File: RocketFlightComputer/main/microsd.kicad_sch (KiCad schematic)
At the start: 1 part

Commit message: Well I added a bunch of sensors, some connectors for battery, pyro channels mosfets, etc
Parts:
- J?: value Micro_SD_Card_Det1 -> Micro_SD_Card
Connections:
- net VDD renamed +3.3V
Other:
- note added: "Max current: 150 mA"
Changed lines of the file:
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@@
   (paper "User" 135.001 119.99)
   (no_connect (at 82.55 34.925))
+  (text "Max current: 150 mA" (at 89.535 74.295 0)
+    (effects (font (size 1.778 1.5113)) (justify left bottom))
+  )
   (hierarchical_label "SD_B0_03" (shape input) (at 82.55 40.005 0) (fields_autoplaced)
     (effects (font (size 1.27 1.27)) (justify left))
@@
   )
   (hierarchical_label "SD_B0_02" (shape input) (at 82.55 42.545 0) (fields_autoplaced)
-    (effects (font (size 1.27 1.27)) (justify left))
-  )
-  (hierarchical_label "VDD" (shape input) (at 82.55 50.165 0) (fields_autoplaced)
     (effects (font (size 1.27 1.27)) (justify left))
   )
@@
     )
   )
+  (symbol (lib_id "power:+3.3V") (at 82.55 50.165 270) (unit 1)
+    (in_bom yes) (on_board yes) (dnp no)
+    (property "Reference" "#PWR059" (at 78.74 50.165 0)
+      (effects (font (size 1.27 1.27)) hide)
+    )
+    (property "Value" "+3.3V" (at 85.725 50.165 90)
+      (effects (font (size 1.27 1.27)) (justify left))
+    )
+    (property "Footprint" "" (at 82.55 50.165 0)
+      (effects (font (size 1.27 1.27)) hide)
+    )
+    (property "Datasheet" "" (at 82.55 50.165 0)
+      (effects (font (size 1.27 1.27)) hide)
+    )
+    (pin "1")
+    (instances
+      (project "main"
+        (path "/27195d1d-92b2-40df-ada5-3b20841577e7"
+          (reference "#PWR059") (unit 1)
+        )
+        (path "/27195d1d-92b2-40df-ada5-3b20841577e7/690c10de-e6bf-48ef-8c3e-99868f905c19"
+          (reference "#PWR0127") (unit 1)
+        )
+      )
+    )
+  )
   (symbol (lib_id "power:GNDREF") (at 82.55 45.085 90) (mirror x) (unit 1)
     (in_bom yes) (on_board yes) (dnp no) (fields_autoplaced)
@@
       (effects (font (size 1.27 1.27)))
     )
-    (property "Value" "Micro_SD_Card_Det1" (at 59.055 29.21 0)
+    (property "Value" "Micro_SD_Card" (at 59.055 29.21 0)
       (effects (font (size 1.27 1.27)))
     )

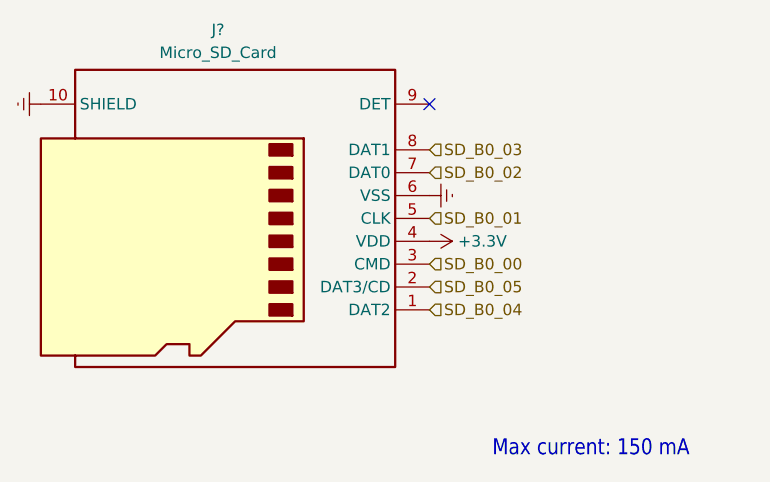
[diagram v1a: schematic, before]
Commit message: Addition of telemetry is pcb schematic
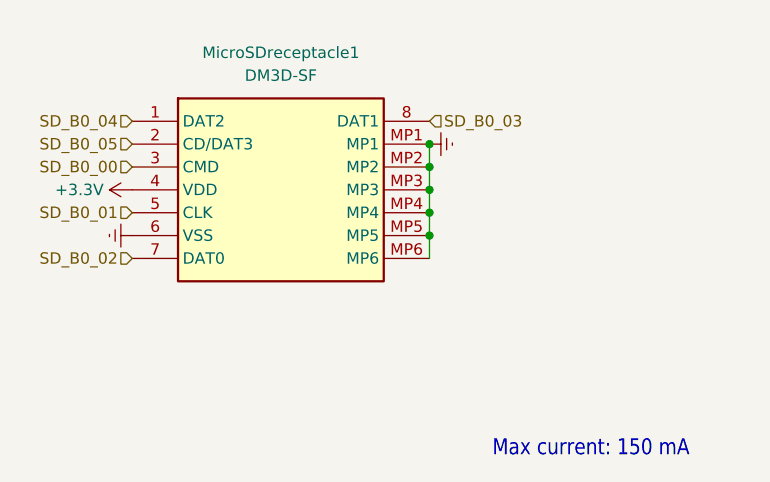
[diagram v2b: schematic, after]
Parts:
- removed J?: Micro_SD_Card, symbol Connector:Micro_SD_Card_Det1
- added MicroSDreceptacle1: DM3D-SF, DM3DSF, symbol DM3D-SF:DM3D-SF
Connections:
- net +3.3V: now also MicroSDreceptacle1.4 (VDD)
- net GNDREF: now also MicroSDreceptacle1.6 (VSS), MicroSDreceptacle1.MP1, MicroSDreceptacle1.MP2, MicroSDreceptacle1.MP3, MicroSDreceptacle1.MP4, MicroSDreceptacle1.MP5, MicroSDreceptacle1.MP6
- net SD_B0_00: now also MicroSDreceptacle1.3 (CMD)
- net SD_B0_01: now also MicroSDreceptacle1.5 (CLK)
- net SD_B0_02: now also MicroSDreceptacle1.7 (DAT0)
- net SD_B0_03: now also MicroSDreceptacle1.8 (DAT1)
- net SD_B0_04: now also MicroSDreceptacle1.1 (DAT2)
- net SD_B0_05: now also MicroSDreceptacle1.2 (CD/DAT3)
- no-connect marks 1 -> 0

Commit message: The design is getting more mature, still did not choose if doing 4 layers or 2 layers pcb, will try to add 5v for a on board camera and trace routes for reserved pins in case of usage on another vehicle
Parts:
- MicroSDreceptacle1: footprint DM3DSF -> DM3DSF:DM3DSF
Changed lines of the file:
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@@
 			)
 		)
-		(property "Footprint" "DM3DSF"
+		(property "Footprint" "DM3DSF:DM3DSF"
 			(at 78.74 131.75 0)
 			(effects

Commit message: Layout of PCB mostly done
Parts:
- DM3D-SF1: renamed from MicroSDreceptacle1; value DM3D-SF -> MicroSD
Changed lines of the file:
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@@
 		(dnp no)
 		(fields_autoplaced yes)
-		(property "Reference" "MicroSDreceptacle1"
+		(property "Reference" "DM3D-SF1"
 			(at 66.04 29.21 0)
 			(effects
@@
 					(size 1.27 1.27)
 				)
+				(hide yes)
 			)
 		)
-		(property "Value" "DM3D-SF"
+		(property "Value" "MicroSD"
 			(at 66.04 31.75 0)
 			(effects
@@
 			(project ""
 				(path "/27195d1d-92b2-40df-ada5-3b20841577e7/690c10de-e6bf-48ef-8c3e-99868f905c19"
-					(reference "MicroSDreceptacle1")
+					(reference "DM3D-SF1")
 					(unit 1)
 				)

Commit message: Addition of all components in BOM, metal mounting plates, need to check psram if its ok for signals to pass under, all components need a double check
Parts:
- DM3D-SF1: LCSC (none) -> C719027
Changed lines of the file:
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@@
 		(on_board yes)
 		(dnp no)
-		(property "Reference" "#PWR0104"
+		(property "Reference" "#PWR0109"
 			(at 53.34 44.45 0)
 			(effects
@@
 			(project "main"
 				(path "/27195d1d-92b2-40df-ada5-3b20841577e7/690c10de-e6bf-48ef-8c3e-99868f905c19"
-					(reference "#PWR0104")
+					(reference "#PWR0109")
 					(unit 1)
 				)
@@
 		(dnp no)
 		(fields_autoplaced yes)
-		(property "Reference" "#PWR0105"
+		(property "Reference" "#PWR0110"
 			(at 43.18 49.53 0)
 			(effects
@@
 			(project "main"
 				(path "/27195d1d-92b2-40df-ada5-3b20841577e7/690c10de-e6bf-48ef-8c3e-99868f905c19"
-					(reference "#PWR0105")
+					(reference "#PWR0110")
 					(unit 1)
 				)
@@
 			)
 		)
+		(property "LCSC" "C719027 "
+			(at 49.53 36.83 0)
+			(effects
+				(font
+					(size 1.27 1.27)
+				)
+				(hide yes)
+			)
+		)
 		(pin "MP1"
 		)
@@
 		(dnp no)
 		(fields_autoplaced yes)
-		(property "Reference" "#PWR0106"
+		(property "Reference" "#PWR0111"
 			(at 88.9 39.37 0)
 			(effects
@@
 			(project "main"
 				(path "/27195d1d-92b2-40df-ada5-3b20841577e7/690c10de-e6bf-48ef-8c3e-99868f905c19"
-					(reference "#PWR0106")
+					(reference "#PWR0111")
 					(unit 1)
 				)
